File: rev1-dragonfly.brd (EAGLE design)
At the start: 49.5 x 34.3 mm, 22 parts, among them J1 USB_MINI-B_SMT, Y1 16MHz

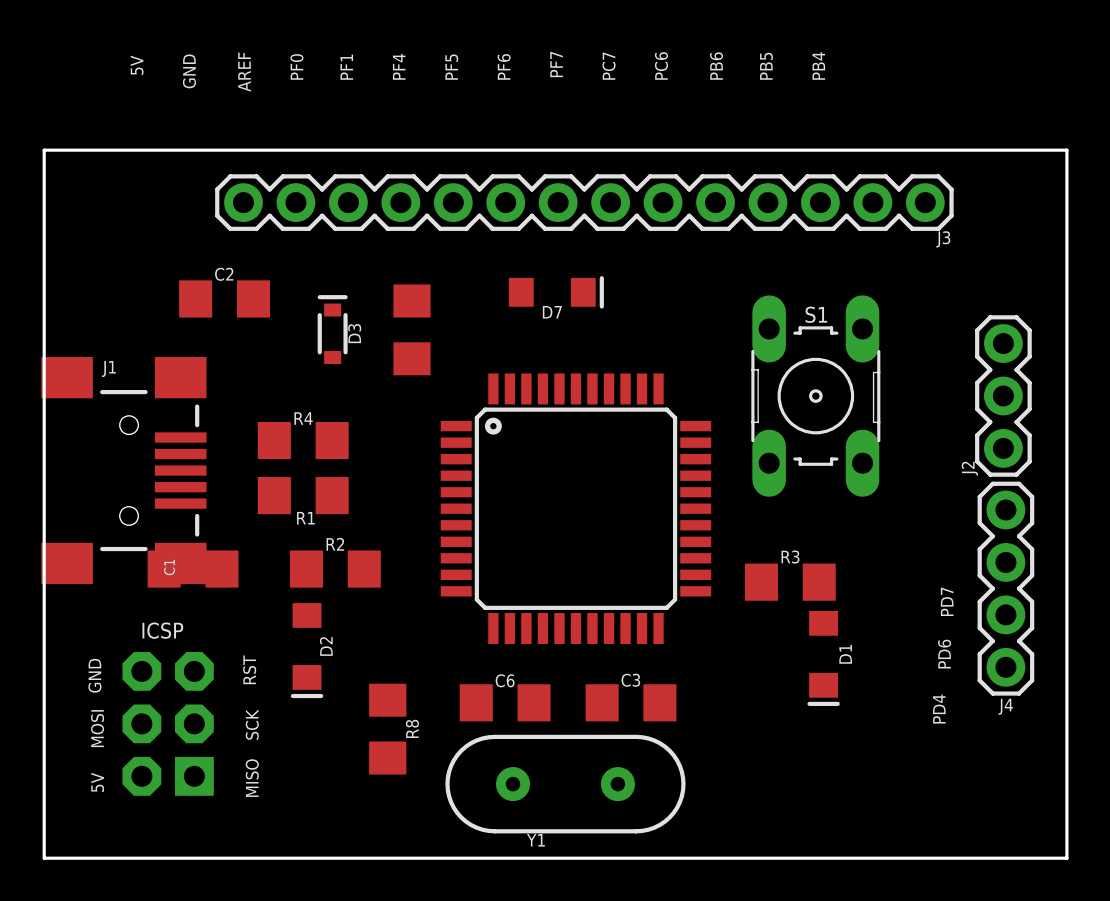
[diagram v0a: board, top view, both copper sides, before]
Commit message: Added proper eagle files
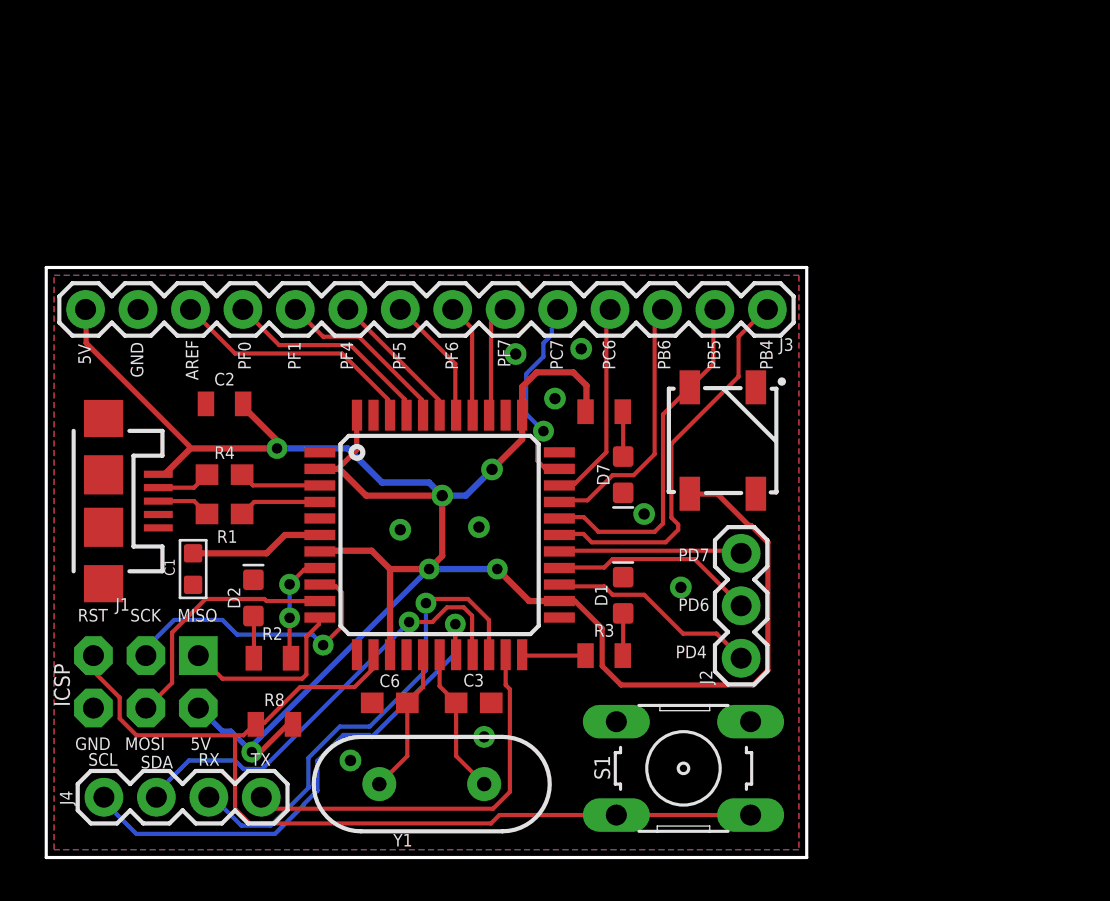
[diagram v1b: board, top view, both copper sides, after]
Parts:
- C1: value 1.0uF -> 1uf; device SparkFun-Capacitors:1206 -> Seeed-Capacitor:C0603
- C2: device SparkFun-Capacitors:1206 -> SparkFun-Capacitors:0805
- C3, C6: device SparkFun-Capacitors:1206 -> SparkFun-Capacitors:0603
- D1, D2, D7: device SparkFun-LED:LED-1206 -> SparkFun-LED:LED-0603
- D3: value 250mA/100V -> WS2812B; device SparkFun-DiscreteSemi:SOD-323 -> SparkFun-LED:WS2812B
- J1: value USB_MINI-B_SMT -> (none); device SparkFun-Connectors:USB-MINIB -> SparkFun-Connectors:USB-MICROB
- R1, R4: value 22 -> 22; device SparkFun-Resistors:1206 -> SparkFun-Resistors:0603
- R2, R7, R8: device SparkFun-Resistors:1206 -> SparkFun-Resistors:0805
- R3: value 1k -> 1k; device SparkFun-Resistors:1206 -> SparkFun-Resistors:0805
- moved J4 44.1 mm to (2.89, 2.95), turned to 0 degrees
- moved D3 19.6 mm to (32.9, 20.2)
- moved S1 19.1 mm to (31.0, 4.35), turned to 180 degrees
- moved J2 16.3 mm to (33.8, 9.68)
- moved D1 10.1 mm to (28.0, 12.7), turned to 90 degrees
- moved R7 10.1 mm to (27.1, 21.6), turned to 180 degrees
- moved R3 9.69 mm to (27.1, 9.81)
- moved D7 9.47 mm to (28.0, 18.6), turned to 270 degrees
- moved J3 9.23 mm to (35.0, 26.6)
- moved C3 7.62 mm to (20.8, 7.53)
- moved U$1 6.73 mm to (19.1, 15.7)
- moved Y1 6.48 mm to (18.8, 3.59)
- moved C6 5.59 mm to (16.7, 7.53)
- moved R8 5.49 mm to (11.1, 6.48), turned to 0 degrees
- moved R2 5.29 mm to (11.1, 9.68)
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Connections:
- net 5V: now also D3.1; no longer D3.C
- net GND: now also D3.3, J1.MT1, J1.MT2, J1.P$1, J1.P$2; no longer D3.A, J1.S1, J1.S2, J1.S3, J1.S4
- net PB5: now also D3.4
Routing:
- net 5V: track 0.00 -> 112.1 mm, vias 0 -> 6
- net RST: track 0.00 -> 47.3 mm
- net PD0: track 0.00 -> 25.4 mm, vias 0 -> 1
- net RX: track 0.00 -> 23.6 mm, vias 0 -> 1
- net PD1: track 0.00 -> 21.6 mm, vias 0 -> 1
- net TX: track 0.00 -> 19.3 mm
- net PB4: track 0.00 -> 19.0 mm
- net PB5: track 0.00 -> 17.0 mm
- net SCK: track 0.00 -> 14.2 mm, vias 0 -> 1
- net PB6: track 0.00 -> 12.8 mm
- net AREF: track 0.00 -> 12.2 mm
- net MOSI: track 0.00 -> 12.1 mm
- net PF0: track 0.00 -> 10.5 mm
- net PD4: track 0.00 -> 10.3 mm
- net PC6: track 0.00 -> 9.99 mm
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- added copper zone on layer 1, net GND
- added copper zone on layer 16, net GND
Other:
- board size 49.5 x 34.3 mm -> 36.8 x 28.6 mm
